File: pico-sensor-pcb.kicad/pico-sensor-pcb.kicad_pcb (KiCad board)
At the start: 2 copper layers, 46 x 60 mm, 9 parts, among them J10 Conn_PCB_2, J11 Conn_I2C1, J13 Conn_I2C1, J7 Conn_PCB_1

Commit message: (very) initial pcb-layout for sensor-board
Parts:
- added C1: 100nF, Capacitor_SMD:C_0402_1005Metric, F.Cu at (119.2, 110.8)
- added C2: 10µF, Capacitor_SMD:C_0603_1608Metric, F.Cu at (117.6, 111.3)
- added C3: 100nF, Capacitor_SMD:C_0402_1005Metric, F.Cu at (102.2, 114.0)
- added C4: 10µF, Capacitor_SMD:C_0603_1608Metric, F.Cu at (102.0, 110.8)
- added C5: 1µF, Capacitor_SMD:C_0603_1608Metric, F.Cu at (140.5, 112.8)
- added D1: LED green, LED_SMD:LED_0805_2012Metric, F.Cu at (130.8, 157.8)
- added D2: LED red, LED_SMD:LED_0805_2012Metric, F.Cu at (107.3, 157.9)
- added JP1: JP_ADDR, Jumper:SolderJumper-2_P1.3mm_Open_Pad1.0x1.5mm, F.Cu at (135.2, 111.3)
- added JP2: JP_Power, Jumper:SolderJumper-2_P1.3mm_Open_Pad1.0x1.5mm, F.Cu at (130.8, 151.9)
- added MK1: MP34DT05TR, user:MP34DT05TR, F.Cu at (106.5, 112.2)
- added R1: 220Ω, Resistor_SMD:R_0402_1005Metric, F.Cu at (119.5, 113.7)
- added R2: 10K, Resistor_SMD:R_0402_1005Metric, F.Cu at (102.3, 116.5)
- added R3: 1K, Resistor_SMD:R_0402_1005Metric, F.Cu at (136.8, 118.3)
- added R4: 10K, Resistor_SMD:R_0402_1005Metric, F.Cu at (140.9, 116.7)
- added R5: 150Ω, Resistor_SMD:R_0402_1005Metric, F.Cu at (130.8, 154.9)
- added R6: 330Ω, Resistor_SMD:R_0402_1005Metric, F.Cu at (107.3, 155.6)
- added SW1: SW_Push, Button_Switch_SMD:SW_SPST_B3S-1000, F.Cu at (105.7, 134.8)
- added SW2: SW_Push, Button_Switch_SMD:SW_SPST_B3S-1000, F.Cu at (105.7, 142.4)
- added SW3: SW_Push, Button_Switch_SMD:SW_SPST_B3S-1000, F.Cu at (105.7, 150.1)
- added SW4: SW_Push, Button_Switch_SMD:SW_SPST_B3S-1000, F.Cu at (136.0, 154.7)
- added SW5: SW_Push, Button_Switch_SMD:SW_SPST_B3S-1000, F.Cu at (125.1, 154.7)
- added U1: AHT20, user:AHT20, F.Cu at (122.7, 111.9)
- added U2: BH1750FVI-TR, user:BH1750, F.Cu at (135.1, 115.2)
- G***: moved to F.Cu
- J10: footprint Connector_JST:JST_SUR_SM08B-SURS-TF_1x08-1MP_P0.80mm_Horizontal -> Connector_JST:JST_SUR_BM08B-SURS-TF_1x08-1MP_P0.80mm_Vertical; moved to B.Cu
- J11: moved to B.Cu
- J13: footprint Connector_PinHeader_2.54mm:PinHeader_1x04_P2.54mm_Vertical -> Connector_PinHeader_2.54mm:PinHeader_1x04_P2.54mm_Horizontal; moved to B.Cu
- J7: footprint Connector_JST:JST_SUR_SM04B-SURS-TF_1x04-1MP_P0.80mm_Horizontal -> Connector_JST:JST_SUR_BM04B-SURS-TF_1x04-1MP_P0.80mm_Vertical; moved to B.Cu
- moved J13 14.6 mm to (138.2, 104.8), turned to 90 degrees
- moved G*** 13.3 mm to (123.2, 129.6), turned to 0 degrees
- moved J10 5.90 mm to (102.3, 131.5)
- moved J7 3.00 mm to (117.2, 157.7), turned to 180 degrees
- moved J11 0.60 mm to (123.0, 103.3), turned to 0 degrees
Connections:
- J10 pad 5: /SDA -> /SWB
- J10 pad 6: /SCL -> /SDA
- J10 pad 7: /SWB -> /SCL
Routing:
- net /SWD: track 0.00 -> 29.0 mm, vias 0 -> 1
- net /RUN: track 0.00 -> 26.0 mm, vias 0 -> 1
- net /SWC: track 0.00 -> 22.1 mm, vias 0 -> 1
- net /~{ON}: track 0.00 -> 16.2 mm, vias 0 -> 1
- net /SWA: track 0.00 -> 11.7 mm, vias 0 -> 1
- net /SWB: track 0.00 -> 9.97 mm, vias 0 -> 1
- net Net-(JP2-Pad2): track 0.00 -> 1.84 mm
- net Net-(D2-Pad2): track 0.00 -> 1.62 mm
- net Net-(D1-Pad2): track 0.00 -> 1.45 mm
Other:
- outline, holes or cut-outs redrawn
- board text added: "A"
- board text added: "B"
- board text added: "C"
- board text added: "Lx"
- board text added: "Mic"
- board text added: "ON"
- board text added: "RST"
- board text added: "https://github.com/bablokb/pcb-pico-datalogger https://opendeved.net/ilce Rev 0.51"
- board text added: "°C"
- board text removed: "I2C1"

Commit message: Rev 0.7: ready for review
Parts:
- added C6: 100nF, Capacitor_SMD:C_0402_1005Metric, F.Cu at (135.7, 113.8)
- added J1: Conn_PDM, Connector_PinHeader_2.54mm:PinHeader_1x04_P2.54mm_Vertical, B.Cu at (109.2, 104.8)
- added J2: Conn_RUN_ON, Connector_PinHeader_2.54mm:PinHeader_1x02_P2.54mm_Vertical, B.Cu at (143.1, 149.6)
- added U3: SCD40_Breakout, user:SCD40_Breakout, F.Cu at (113.8, 119.8)
- added U4: ENS160_Breakout, user:ENS160_Breakout, F.Cu at (130.3, 144.7)
- G***: moved to B.Cu
- moved C2 8.77 mm to (125.9, 108.5), turned to 0 degrees
- moved C1 7.60 mm to (126.8, 110.5), turned to -90 degrees
- moved C5 7.05 mm to (133.5, 113.6)
- moved R4 6.62 mm to (137.8, 110.8), turned to 90 degrees
- moved G*** 6.16 mm to (122.4, 123.5), turned to 180 degrees
- moved R1 6.12 mm to (122.7, 108.5), turned to 90 degrees
- moved R2 5.31 mm to (107.0, 114.1), turned to -90 degrees
- moved C4 4.73 mm to (106.8, 111.4), turned to -90 degrees
- moved JP1 4.60 mm to (139.1, 113.7), turned to -90 degrees
- moved R3 4.55 mm to (136.8, 113.8), turned to 90 degrees
- moved C3 4.25 mm to (105.3, 111.1), turned to -90 degrees
- moved U2 3.61 mm to (135.3, 111.7)
- moved MK1 3.10 mm to (109.6, 112.2)
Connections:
- C1 pad 1: +3V3 -> Net-(C1-Pad1)
- C2 pad 1: +3V3 -> Net-(C1-Pad1)
- R1 pad 1: Net-(R1-Pad1) -> Net-(C1-Pad1)
- U1 pad 2: Net-(R1-Pad1) -> Net-(C1-Pad1)
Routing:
- net +3V3: track 0.00 -> 179.3 mm, vias 0 -> 4
- net /SCL: track 0.00 -> 78.7 mm, vias 0 -> 1
- net /SDA: track 0.00 -> 68.7 mm, vias 0 -> 1
- net /PDM_DAT: track 0.00 -> 33.6 mm, vias 0 -> 1
- net /PDM_CLK: track 0.00 -> 31.5 mm, vias 0 -> 1
- net /~{ON}: track 16.2 -> 37.6 mm, vias 1 -> 2
- net /RUN: track 26.0 -> 35.8 mm
- net Net-(C5-Pad2): track 0.00 -> 9.56 mm
- net Net-(C1-Pad1): track 0.00 -> 9.14 mm, vias 0 -> 2
- net /SWB: track 9.97 -> 17.9 mm
- net Net-(JP1-Pad1): track 0.00 -> 3.61 mm
- net Net-(MK1-Pad2): track 0.00 -> 3.05 mm
- net /SWD: track 29.0 -> 31.5 mm
- net GND: track 0.00 -> 1.57 mm, vias 0 -> 11
- added copper zone on B.Cu, net GND
- added copper zone on F.Cu, net GND
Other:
- board text added: "3V3"
- board text added: "GND"
- board text added: "PDM_CLK"
- board text added: "PDM_DAT"
- board text added: "SCL"
- board text added: "SDA"
- board text added: "https://github.com/bablokb/pcb-pico-datalogger https://opendeved.net/ilce Rev 0.70"
- board text removed: "https://github.com/bablokb/pcb-pico-datalogger https://opendeved.net/ilce Rev 0.51"

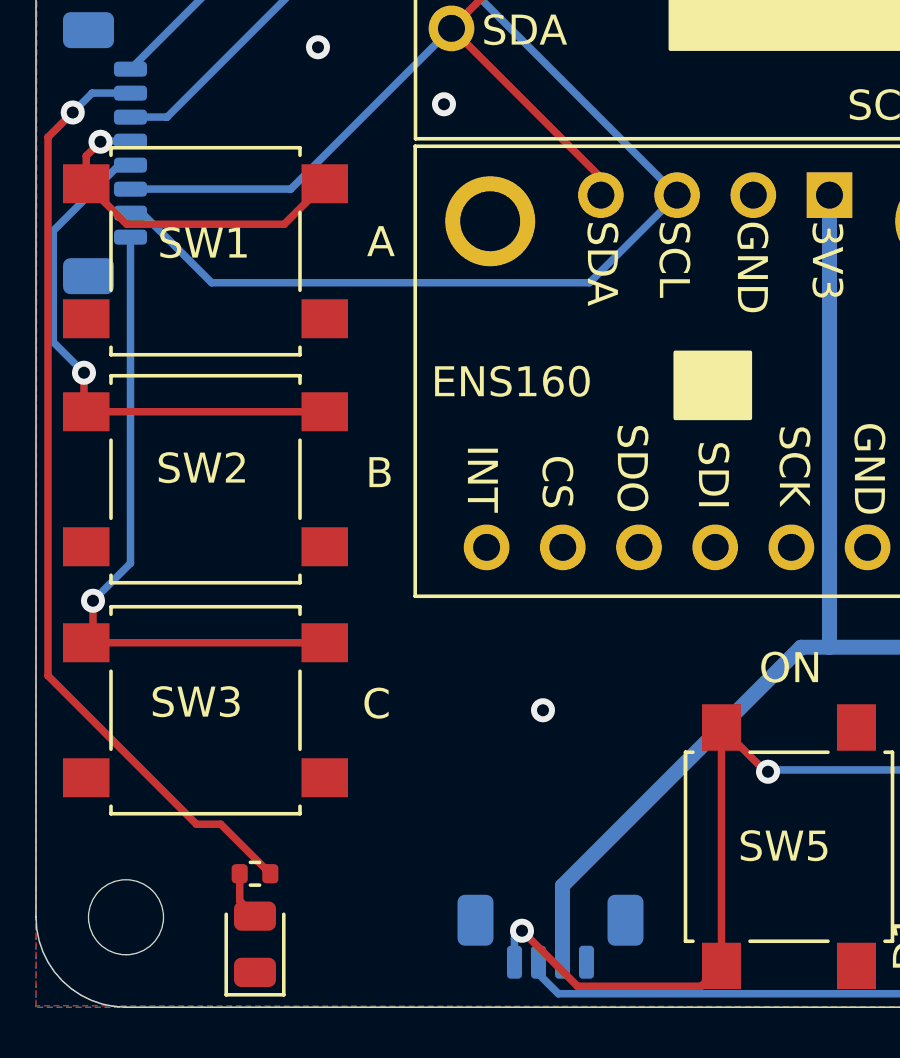
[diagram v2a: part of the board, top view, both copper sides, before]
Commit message: add compatibility-connector for application-controls (A-D)
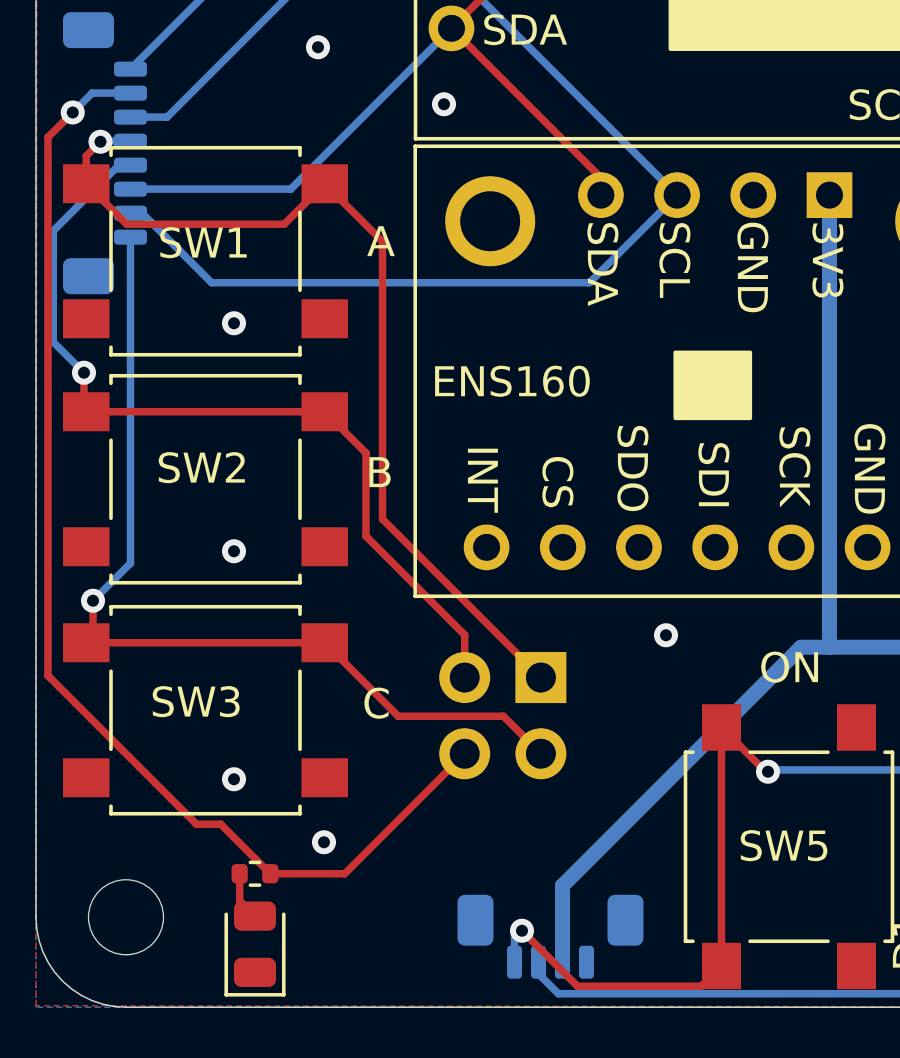
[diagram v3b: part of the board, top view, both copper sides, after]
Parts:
- added J3: Conn_Controls, Connector_PinHeader_2.54mm:PinHeader_2x02_P2.54mm_Vertical, B.Cu at (116.8, 149.0)
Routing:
- net /SWA: track 11.7 -> 31.1 mm
- net /SWB: track 17.9 -> 28.7 mm
- net /SWC: track 22.1 -> 30.8 mm
- net /SWD: track 31.5 -> 39.6 mm
- net GND: vias 11 -> 15
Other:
- board text added: "D"
- board text added: "https://github.com/bablokb/pcb-pico-datalogger https://opendeved.net/ilce Rev 0.71"
- board text removed: "https://github.com/bablokb/pcb-pico-datalogger https://opendeved.net/ilce Rev 0.70"
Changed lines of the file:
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@@
+    )
+  )
+  (footprint "Connector_PinHeader_2.54mm:PinHeader_2x02_P2.54mm_Vertical" (layer "B.Cu")
+    (at 116.83 149.01 180)
+    (descr "Through hole straight pin header, 2x02, 2.54mm pitch, double rows")
+    (tags "Through hole pin header THT 2x02 2.54mm double row")
+    (property "Sheetfile" "pico-sensor-pcb.kicad_sch")
+    (property "Sheetname" "")
+    (attr through_hole)
+    (fp_text reference "J3" (at 1.27 2.33) (layer "B.SilkS") hide
+      (effects (font (size 1 1) (thickness 0.15)) (justify mirror))
+    )
+    (fp_text value "Conn_Controls" (at 1.27 -4.87) (layer "B.Fab") hide
+      (effects (font (size 1 1) (thickness 0.15)) (justify mirror))
+    )
+    (fp_text user "${REFERENCE}" (at 1.27 -1.27 90) (layer "B.Fab")
+      (effects (font (size 1 1) (thickness 0.15)) (justify mirror))
+    )
+    (fp_line (start -1.33 1.33) (end 0 1.33) (layer "B.SilkS") (width 0.12))
+    (fp_line (start -1.33 0) (end -1.33 1.33) (layer "B.SilkS") (width 0.12))
+    (fp_line (start 3.87 1.33) (end 3.87 -3.87) (layer "B.SilkS") (width 0.12))
+    (fp_line (start -1.33 -1.27) (end 1.27 -1.27) (layer "B.SilkS") (width 0.12))
+    (fp_line (start 1.27 -1.27) (end 1.27 1.33) (layer "B.SilkS") (width 0.12))
+    (fp_line (start 1.27 1.33) (end 3.87 1.33) (layer "B.SilkS") (width 0.12))
+    (fp_line (start -1.33 -1.27) (end -1.33 -3.87) (layer "B.SilkS") (width 0.12))
+    (fp_line (start -1.33 -3.87) (end 3.87 -3.87) (layer "B.SilkS") (width 0.12))
+    (fp_line (start -1.8 -4.35) (end 4.35 -4.35) (layer "B.CrtYd") (width 0.05))
+    (fp_line (start 4.35 1.8) (end -1.8 1.8) (layer "B.CrtYd") (width 0.05))
+    (fp_line (start 4.35 -4.35) (end 4.35 1.8) (layer "B.CrtYd") (width 0.05))
+    (fp_line (start -1.8 1.8) (end -1.8 -4.35) (layer "B.CrtYd") (width 0.05))
+    (fp_line (start -1.27 -3.81) (end -1.27 0) (layer "B.Fab") (width 0.1))
+    (fp_line (start 3.81 -3.81) (end -1.27 -3.81) (layer "B.Fab") (width 0.1))
+    (fp_line (start 3.81 1.27) (end 3.81 -3.81) (layer "B.Fab") (width 0.1))
+    (fp_line (start 0 1.27) (end 3.81 1.27) (layer "B.Fab") (width 0.1))
+    (fp_line (start -1.27 0) (end 0 1.27) (layer "B.Fab") (width 0.1))
+    (pad "1" thru_hole rect (at 0 0 180) (size 1.7 1.7) (drill 1) (layers *.Cu *.Mask)
+      (net 15 "/SWA") (pinfunction "Pin_1") (pintype "passive"))
+    (pad "2" thru_hole oval (at 2.54 0 180) (size 1.7 1.7) (drill 1) (layers *.Cu *.Mask)
+      (net 16 "/SWB") (pinfunction "Pin_2") (pintype "passive"))
+    (pad "3" thru_hole oval (at 0 -2.54 180) (size 1.7 1.7) (drill 1) (layers *.Cu *.Mask)
+      (net 17 "/SWC") (pinfunction "Pin_3") (pintype "passive"))
+    (pad "4" thru_hole oval (at 2.54 -2.54 180) (size 1.7 1.7) (drill 1) (layers *.Cu *.Mask)
+      (net 9 "/SWD") (pinfunction "Pin_4") (pintype "passive"))
+    (model "${KICAD6_3DMODEL_DIR}/Connector_PinHeader_2.54mm.3dshapes/PinHeader_2x02_P2.54mm_Vertical.wrl"
+      (offset (xyz 0 0 0))
+      (scale (xyz 1 1 1))
+      (rotate (xyz 0 0 0))
     )
   )
@@
   (gr_arc (start 143 100) (mid 145.12132 100.87868) (end 146 103) (layer "Edge.Cuts") (width 0.05))
   (gr_arc (start 100 103) (mid 100.87868 100.87868) (end 103 100) (layer "Edge.Cuts") (width 0.05))
+  (gr_text "C" (at 116.9 154.1) (layer "B.SilkS")
+    (effects (font (size 1 1) (thickness 0.15)) (justify mirror))
+  )
+  (gr_text "B" (at 114.3 146.6) (layer "B.SilkS")
+    (effects (font (size 1 1) (thickness 0.15)) (justify mirror))
+  )
   (gr_text "PCB2" (at 111.75 156.55) (layer "B.SilkS")
     (effects (font (size 0.9 0.9) (thickness 0.15)) (justify mirror))
@@
     (effects (font (size 1 1) (thickness 0.15)) (justify mirror))
   )
-  (gr_text "https://github.com/bablokb/pcb-pico-datalogger\nhttps://opendeved.net/ilce               Rev 0.70" (at 143.65 107.25 90) (layer "B.SilkS")
+  (gr_text "https://github.com/bablokb/pcb-pico-datalogger\nhttps://opendeved.net/ilce               Rev 0.71" (at 143.65 107.25 90) (layer "B.SilkS")
     (effects (font (size 1 1) (thickness 0.15)) (justify left mirror))
   )
+  (gr_text "D" (at 114.3 154.2) (layer "B.SilkS")
+    (effects (font (size 1 1) (thickness 0.15)) (justify mirror))
+  )
   (gr_text "SDA" (at 133.25 107.473809 90) (layer "B.SilkS")
     (effects (font (size 1 1) (thickness 0.15)) (justify mirror))
   )
   (gr_text "PDM_DAT" (at 111.9 109.580952 90) (layer "B.SilkS")
+    (effects (font (size 1 1) (thickness 0.15)) (justify mirror))
+  )
+  (gr_text "A" (at 116.8 146.6) (layer "B.SilkS")
     (effects (font (size 1 1) (thickness 0.15)) (justify mirror))
   )
@@
   (segment (start 136.99 111.15) (end 137.85 110.29) (width 0.25) (layer "F.Cu") (net 1))
   (segment (start 136.6375 111.15) (end 136.99 111.15) (width 0.25) (layer "F.Cu") (net 1))
-  (via (at 116.9 150.1) (size 0.8) (drill 0.4) (layers "F.Cu" "B.Cu") (free) (net 1))
+  (via (at 121 147.6) (size 0.8) (drill 0.4) (layers "F.Cu" "B.Cu") (free) (net 1))
+  (via (at 109.6 154.5) (size 0.8) (drill 0.4) (layers "F.Cu" "B.Cu") (free) (net 1))
+  (via (at 106.6 144.8) (size 0.8) (drill 0.4) (layers "F.Cu" "B.Cu") (free) (net 1))
   (via (at 106 118.7) (size 0.8) (drill 0.4) (layers "F.Cu" "B.Cu") (free) (net 1))
   (via (at 144.8 106.1) (size 0.8) (drill 0.4) (layers "F.Cu" "B.Cu") (free) (net 1))
   (via (at 109.1 124.1) (size 0.8) (drill 0.4) (layers "F.Cu" "B.Cu") (free) (net 1))
+  (via (at 106.6 137.2) (size 0.8) (drill 0.4) (layers "F.Cu" "B.Cu") (free) (net 1))
   (via (at 137.8 131.7) (size 0.8) (drill 0.4) (layers "F.Cu" "B.Cu") (free) (net 1))
   (via (at 114.8 113.2) (size 0.8) (drill 0.4) (layers "F.Cu" "B.Cu") (free) (net 1))
+  (via (at 106.6 152.4) (size 0.8) (drill 0.4) (layers "F.Cu" "B.Cu") (free) (net 1))
   (via (at 136.4 156.3) (size 0.8) (drill 0.4) (layers "F.Cu" "B.Cu") (free) (net 1))
   (via (at 113.6 129.9) (size 0.8) (drill 0.4) (layers "F.Cu" "B.Cu") (free) (net 1))
@@
   (segment (start 111.85 107.375) (end 111.85 110.124695) (width 0.25) (layer "B.Cu") (net 8))
   (segment (start 103.15 128.73) (end 111.8 120.08) (width 0.25) (layer "B.Cu") (net 8))
+  (segment (start 107.81 155.55) (end 110.29 155.55) (width 0.25) (layer "F.Cu") (net 9))
   (segment (start 100.4 148.95) (end 105.35 153.9) (width 0.25) (layer "F.Cu") (net 9))
   (segment (start 106.16 153.9) (end 107.81 155.55) (width 0.25) (layer "F.Cu") (net 9))
   (segment (start 100.4 131) (end 100.4 148.95) (width 0.25) (layer "F.Cu") (net 9))
+  (segment (start 110.29 155.55) (end 114.29 151.55) (width 0.25) (layer "F.Cu") (net 9))
   (segment (start 105.35 153.9) (end 106.16 153.9) (width 0.25) (layer "F.Cu") (net 9))
   (segment (start 101.225 130.175) (end 100.4 131) (width 0.25) (layer "F.Cu") (net 9))
@@
   (segment (start 107 114.61) (end 107.64 114.61) (width 0.1) (layer "F.Cu") (net 13))
   (segment (start 101.675 132.55) (end 103.025 133.9) (width 0.25) (layer "F.Cu") (net 15))
+  (segment (start 111.55 143.73) (end 111.55 134.475) (width 0.25) (layer "F.Cu") (net 15))
   (segment (start 103.025 133.9) (end 108.275 133.9) (width 0.25) (layer "F.Cu") (net 15))
+  (segment (start 116.83 149.01) (end 111.55 143.73) (width 0.25) (layer "F.Cu") (net 15))
   (segment (start 101.675 131.625) (end 101.675 132.55) (width 0.25) (layer "F.Cu") (net 15))
   (segment (start 102.15 131.15) (end 101.675 131.625) (width 0.25) (layer "F.Cu") (net 15))
+  (segment (start 111.55 134.475) (end 109.625 132.55) (width 0.25) (layer "F.Cu") (net 15))
   (segment (start 108.275 133.9) (end 109.625 132.55) (width 0.25) (layer "F.Cu") (net 15))
   (via (at 102.15 131.15) (size 0.8) (drill 0.4) (layers "F.Cu" "B.Cu") (net 15))
   (segment (start 103.15 131.13) (end 102.17 131.13) (width 0.25) (layer "B.Cu") (net 15))
   (segment (start 102.17 131.13) (end 102.15 131.15) (width 0.25) (layer "B.Cu") (net 15))
+  (segment (start 111 144.3) (end 111 141.525) (width 0.25) (layer "F.Cu") (net 16))
   (segment (start 109.625 140.15) (end 101.675 140.15) (width 0.25) (layer "F.Cu") (net 16))
+  (segment (start 114.29 147.59) (end 111 144.3) (width 0.25) (layer "F.Cu") (net 16))
+  (segment (start 114.29 149.01) (end 114.29 147.59) (width 0.25) (layer "F.Cu") (net 16))
   (segment (start 101.6 140.075) (end 101.675 140.15) (width 0.25) (layer "F.Cu") (net 16))
   (segment (start 101.6 138.85) (end 101.6 140.075) (width 0.25) (layer "F.Cu") (net 16))
+  (segment (start 111 141.525) (end 109.625 140.15) (width 0.25) (layer "F.Cu") (net 16))
   (via (at 101.6 138.85) (size 0.8) (drill 0.4) (layers "F.Cu" "B.Cu") (net 16))
   (segment (start 100.575 137.825) (end 100.575 134.118604) (width 0.25) (layer "B.Cu") (net 16))
@@
   (segment (start 102.763604 131.93) (end 103.15 131.93) (width 0.25) (layer "B.Cu") (net 16))
   (segment (start 100.575 134.118604) (end 102.763604 131.93) (width 0.25) (layer "B.Cu") (net 16))
+  (segment (start 116.83 151.55) (end 115.58 150.3) (width 0.25) (layer "F.Cu") (net 17))
+  (segment (start 112.075 150.3) (end 109.625 147.85) (width 0.25) (layer "F.Cu") (net 17))
   (segment (start 101.9 146.45) (end 101.9 147.625) (width 0.25) (layer "F.Cu") (net 17))
+  (segment (start 115.58 150.3) (end 112.075 150.3) (width 0.25) (layer "F.Cu") (net 17))
   (segment (start 109.625 147.85) (end 101.675 147.85) (width 0.25) (layer "F.Cu") (net 17))
   (segment (start 101.9 147.625) (end 101.675 147.85) (width 0.25) (layer "F.Cu") (net 17))

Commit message: Rev. 0.80: fixed PCB-connectors
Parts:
- turned J10 to 90 degrees
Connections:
- J10 pad 1: /PDM_CLK -> /SWC
- J10 pad 2: /SWD -> /SCL
- J10 pad 3: /PDM_DAT -> /SDA
- J10 pad 4: /SWA -> /SWB
- J10 pad 5: /SWB -> /SWA
- J10 pad 6: /SDA -> /PDM_DAT
- J10 pad 7: /SCL -> /SWD
- J10 pad 8: /SWC -> /PDM_CLK
- J7 pad 1: GND -> /~{ON}
- J7 pad 2: +3V3 -> /RUN
- J7 pad 3: /RUN -> +3V3
- J7 pad 4: /~{ON} -> GND
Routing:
- net /~{ON}: track 37.6 -> 33.3 mm
- net /PDM_DAT: track 33.6 -> 35.9 mm
- net /PDM_CLK: track 31.5 -> 33.7 mm
- net /SCL: track 78.7 -> 80.4 mm
- net /SDA: track 68.7 -> 70.4 mm
- net /SWD: track 39.6 -> 38.7 mm
- net /SWC: track 30.8 -> 31.5 mm
- net /SWB: track 28.7 -> 28.0 mm
- net /RUN: track 35.8 -> 35.2 mm
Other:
- board text added: "https://github.com/bablokb/pcb-pico-datalogger https://opendeved.net/ilce Rev 0.80"
- board text removed: "https://github.com/bablokb/pcb-pico-datalogger https://opendeved.net/ilce Rev 0.71"

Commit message: Rev: 0.90: minor CPL fixes
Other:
- board text added: "https://github.com/bablokb/pcb-pico-datalogger https://opendeved.net/ilce Rev 0.90"
- board text removed: "https://github.com/bablokb/pcb-pico-datalogger https://opendeved.net/ilce Rev 0.80"
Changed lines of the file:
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@@
     (effects (font (size 1 1) (thickness 0.15)) (justify mirror))
   )
-  (gr_text "PCB2" (at 111.75 156.55) (layer "B.SilkS")
+  (gr_text "PCB1" (at 111.75 156.55) (layer "B.SilkS")
     (effects (font (size 0.9 0.9) (thickness 0.15)) (justify mirror))
   )
@@
     (effects (font (size 1 1) (thickness 0.15)) (justify mirror))
   )
-  (gr_text "https://github.com/bablokb/pcb-pico-datalogger\nhttps://opendeved.net/ilce               Rev 0.80" (at 143.65 107.25 90) (layer "B.SilkS")
+  (gr_text "https://github.com/bablokb/pcb-pico-datalogger\nhttps://opendeved.net/ilce               Rev 0.90" (at 143.65 107.25 90) (layer "B.SilkS")
     (effects (font (size 1 1) (thickness 0.15)) (justify left mirror))
   )
@@
     (effects (font (size 1 1) (thickness 0.15)) (justify mirror))
   )
-  (gr_text "PCB1" (at 102.4 125.63) (layer "B.SilkS")
+  (gr_text "PCB2" (at 102.4 125.63) (layer "B.SilkS")
     (effects (font (size 0.9 0.9) (thickness 0.15)) (justify mirror))
   )
